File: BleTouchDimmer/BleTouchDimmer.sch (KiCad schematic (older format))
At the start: 12 parts, among them P1 PROG, P2 UART, U2 MDBT40, Y2 Crystal

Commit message: Added triacs.
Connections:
- wire segments 59 -> 55
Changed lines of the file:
@@
 	3650 3550 3650 3600
 $Comp
-L GND #PWR2
+L GND #PWR01
 U 1 1 57955487
 P 3100 3950
-F 0 "#PWR2" H 3100 3700 50  0001 C CNN
+F 0 "#PWR01" H 3100 3700 50  0001 C CNN
 F 1 "GND" H 3100 3800 50  0000 C CNN
 F 2 "" H 3100 3950 50  0000 C CNN
@@
 $EndComp
 Wire Wire Line
-	3250 4100 3250 3850
-Wire Wire Line
-	3250 3850 3250 3550
+	3250 3550 3250 4100
 Wire Wire Line
 	3100 3850 3250 3850
@@
 $EndComp
 $Comp
-L GND #PWR4
+L GND #PWR02
 U 1 1 581A3066
 P 4250 2800
-F 0 "#PWR4" H 4250 2550 50  0001 C CNN
+F 0 "#PWR02" H 4250 2550 50  0001 C CNN
 F 1 "GND" H 4250 2650 50  0000 C CNN
 F 2 "" H 4250 2800 50  0000 C CNN
@@
 $EndComp
 $Comp
-L GND #PWR10
+L GND #PWR03
 U 1 1 581A31E1
 P 6950 2650
-F 0 "#PWR10" H 6950 2400 50  0001 C CNN
+F 0 "#PWR03" H 6950 2400 50  0001 C CNN
 F 1 "GND" H 6950 2500 50  0000 C CNN
 F 2 "" H 6950 2650 50  0000 C CNN
@@
 	4400 2650 4250 2650
 Wire Wire Line
-	4250 2650 4250 2750
-Wire Wire Line
-	4250 2750 4250 2800
+	4250 2650 4250 2800
 Wire Wire Line
 	4400 2750 4250 2750
@@
 	3100 3850 3100 3950
 $Comp
-L GND #PWR5
+L GND #PWR04
 U 1 1 581A7CB9
 P 5000 4750
-F 0 "#PWR5" H 5000 4500 50  0001 C CNN
+F 0 "#PWR04" H 5000 4500 50  0001 C CNN
 F 1 "GND" H 5000 4600 50  0000 C CNN
 F 2 "" H 5000 4750 50  0000 C CNN
@@
 	5000 4550 5000 4750
 $Comp
-L GND #PWR8
+L GND #PWR05
 U 1 1 581A7D2A
 P 6200 4750
-F 0 "#PWR8" H 6200 4500 50  0001 C CNN
+F 0 "#PWR05" H 6200 4500 50  0001 C CNN
 F 1 "GND" H 6200 4600 50  0000 C CNN
 F 2 "" H 6200 4750 50  0000 C CNN
@@
 	6200 4550 6200 4750
 $Comp
-L GND #PWR7
+L GND #PWR06
 U 1 1 581A884C
 P 5000 5900
-F 0 "#PWR7" H 5000 5650 50  0001 C CNN
+F 0 "#PWR06" H 5000 5650 50  0001 C CNN
 F 1 "GND" H 5000 5750 50  0000 C CNN
 F 2 "" H 5000 5900 50  0000 C CNN
@@
 	5000 5800 5000 5900
 $Comp
-L GND #PWR1
+L GND #PWR07
 U 1 1 581ABEA9
 P 3100 3200
-F 0 "#PWR1" H 3100 2950 50  0001 C CNN
+F 0 "#PWR07" H 3100 2950 50  0001 C CNN
 F 1 "GND" H 3100 3050 50  0000 C CNN
 F 2 "" H 3100 3200 50  0000 C CNN
@@
 $EndComp
 Wire Wire Line
-	4400 3100 3850 3100
-Wire Wire Line
-	3850 3100 3550 3100
+	3550 3100 4400 3100
 Wire Wire Line
 	3250 3100 3100 3100
@@
 	3100 3100 3100 3200
 $Comp
-L +3.3V #PWR6
+L +3.3V #PWR08
 U 1 1 581AC6F3
 P 5000 5350
-F 0 "#PWR6" H 5000 5200 50  0001 C CNN
+F 0 "#PWR08" H 5000 5200 50  0001 C CNN
 F 1 "+3.3V" H 5000 5490 50  0000 C CNN
 F 2 "" H 5000 5350 50  0000 C CNN
@@
 $EndComp
 Wire Wire Line
-	5000 5350 5000 5450
-Wire Wire Line
-	5000 5450 5000 5500
+	5000 5350 5000 5500
 Wire Wire Line
 	5100 4550 5100 5450
@@
 Connection ~ 5000 5450
 $Comp
-L +3.3V #PWR3
+L +3.3V #PWR09
 U 1 1 581E4E9B
 P 3850 3050
-F 0 "#PWR3" H 3850 2900 50  0001 C CNN
+F 0 "#PWR09" H 3850 2900 50  0001 C CNN
 F 1 "+3.3V" H 3850 3190 50  0000 C CNN
 F 2 "" H 3850 3050 50  0000 C CNN
@@
 	7800 3850 7800 4000
 $Comp
-L GND #PWR11
+L GND #PWR010
 U 1 1 581AB091
 P 7800 4000
-F 0 "#PWR11" H 7800 3750 50  0001 C CNN
+F 0 "#PWR010" H 7800 3750 50  0001 C CNN
 F 1 "GND" H 7800 3850 50  0000 C CNN
 F 2 "" H 7800 4000 50  0000 C CNN
@@
 SWDIO/RESET
 $Comp
-L +3.3V #PWR12
+L +3.3V #PWR011
 U 1 1 581E9153
 P 9000 3200
-F 0 "#PWR12" H 9000 3050 50  0001 C CNN
+F 0 "#PWR011" H 9000 3050 50  0001 C CNN
 F 1 "+3.3V" H 9000 3340 50  0000 C CNN
 F 2 "" H 9000 3200 50  0000 C CNN
@@
 	9000 3200 9000 3250
 $Comp
-L GND #PWR13
+L GND #PWR012
 U 1 1 581E91BB
 P 9000 3600
-F 0 "#PWR13" H 9000 3350 50  0001 C CNN
+F 0 "#PWR012" H 9000 3350 50  0001 C CNN
 F 1 "GND" H 9000 3450 50  0000 C CNN
 F 2 "" H 9000 3600 50  0000 C CNN
@@
 TX
 $Comp
-L GND #PWR16
+L GND #PWR013
 U 1 1 581EB2A9
 P 9200 5150
-F 0 "#PWR16" H 9200 4900 50  0001 C CNN
+F 0 "#PWR013" H 9200 4900 50  0001 C CNN
 F 1 "GND" H 9200 5000 50  0000 C CNN
 F 2 "" H 9200 5150 50  0000 C CNN
@@
 	10050 4800 9200 4800
 $Comp
-L +3.3V #PWR15
+L +3.3V #PWR014
 U 1 1 581EB479
 P 9200 4750
-F 0 "#PWR15" H 9200 4600 50  0001 C CNN
+F 0 "#PWR014" H 9200 4600 50  0001 C CNN
 F 1 "+3.3V" H 9200 4890 50  0000 C CNN
 F 2 "" H 9200 4750 50  0000 C CNN
@@
 	9000 4850 9000 4900
 $Comp
-L +3.3V #PWR14
+L +3.3V #PWR015
 U 1 1 581EE473
 P 9000 4500
-F 0 "#PWR14" H 9000 4350 50  0001 C CNN
+F 0 "#PWR015" H 9000 4350 50  0001 C CNN
 F 1 "+3.3V" H 9000 4640 50  0000 C CNN
 F 2 "" H 9000 4500 50  0000 C CNN
@@
 	6900 4650 6900 4750
 $Comp
-L GND #PWR9
+L GND #PWR016
 U 1 1 581F1D57
 P 6900 5250
-F 0 "#PWR9" H 6900 5000 50  0001 C CNN
+F 0 "#PWR016" H 6900 5000 50  0001 C CNN
 F 1 "GND" H 6900 5100 50  0000 C CNN
 F 2 "" H 6900 5250 50  0000 C CNN
@@
 ZC_DETECT
 $Comp
-L PWR_FLAG #FLG1
+L PWR_FLAG #FLG017
 U 1 1 581FAA9C
 P 10450 850
-F 0 "#FLG1" H 10450 945 50  0001 C CNN
+F 0 "#FLG017" H 10450 945 50  0001 C CNN
 F 1 "PWR_FLAG" H 10450 1030 50  0000 C CNN
 F 2 "" H 10450 850 50  0000 C CNN
@@
 $EndComp
 $Comp
-L GND #PWR17
+L GND #PWR018
 U 1 1 581FAAED
 P 10450 1150
-F 0 "#PWR17" H 10450 900 50  0001 C CNN
+F 0 "#PWR018" H 10450 900 50  0001 C CNN
 F 1 "GND" H 10450 1000 50  0000 C CNN
 F 2 "" H 10450 1150 50  0000 C CNN
@@
 $EndComp
 $Comp
-L +3.3V #PWR18
+L +3.3V #PWR019
 U 1 1 581FAB37
 P 10800 850
-F 0 "#PWR18" H 10800 700 50  0001 C CNN
+F 0 "#PWR019" H 10800 700 50  0001 C CNN
 F 1 "+3.3V" H 10800 990 50  0000 C CNN
 F 2 "" H 10800 850 50  0000 C CNN
@@
 $EndComp
 $Comp
-L PWR_FLAG #FLG2
+L PWR_FLAG #FLG020
 U 1 1 581FAB81
 P 10800 1100
-F 0 "#FLG2" H 10800 1195 50  0001 C CNN
+F 0 "#FLG020" H 10800 1195 50  0001 C CNN
 F 1 "PWR_FLAG" H 10800 1280 50  0000 C CNN
 F 2 "" H 10800 1100 50  0000 C CNN
@@
 F0 "TRIACS" 60
 F1 "TRIACS.sch" 60
+F2 "TRIAC1_CONTROL" I L 2700 5450 60
+F3 "230VAC_L" I R 3950 5750 60
+F4 "TRIAC1_L_OUT" I R 3950 5900 60
+F5 "TRIAC2_CONTROL" I L 2700 5600 60
+F6 "TRIAC2_L_OUT" I R 3950 6050 60
 $EndSheet
 $EndSCHEMATC

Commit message: Added terminal block.
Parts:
- added P3: POWER, Terminal_Blocks:TerminalBlock_Pheonix_MKDS1.5-4pol, symbol CONN_01X04
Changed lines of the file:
@@
 F6 "TRIAC2_L_OUT" I R 3950 6050 60
 $EndSheet
+$Comp
+L CONN_01X04 P3
+U 1 1 5823D05F
+P 1950 4100
+F 0 "P3" H 1950 4350 50  0000 C CNN
+F 1 "POWER" V 2050 4100 50  0000 C CNN
+F 2 "Terminal_Blocks:TerminalBlock_Pheonix_MKDS1.5-4pol" H 1950 4100 50  0001 C CNN
+F 3 "http://www.mouser.com/ds/2/418/NG_CD_282837_G3-625767.pdf" H 1950 4100 50  0001 C CNN
+F 4 "http://www.mouser.ee/ProductDetail/TE-Connectivity/282837-4/?qs=sGAEpiMZZMvZTcaMAxB2AJ%2f79sE4hFAYNPaLlOiyu2A%3d" H 1950 4100 60  0001 C CNN "Ordering"
+	1    1950 4100
+	-1   0    0    -1
+$EndComp
 $EndSCHEMATC

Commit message: Added comments about possible power supply solutions.
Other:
- note added: "TODO\nPOWERSUPPLY\nPROTECTION\nENCODER/TOUCHWHEEL"
- note added: "http://electronics.stackexchange.com/questions/101818/surface-mount-transformerless-230v-to-3-3v-on-a-small-board"
- note added: "http://electronics.stackexchange.com/questions/67295/converting-universal-ac-to-3-3v-dc-0-1a"
- note added: "http://www.mouser.ee/Semiconductors/Power-Management-ICs/AC-DC-Converters/_/N-64puj/?Ns=Pricing|0"
- note added: "http://www.promelec.ru/pdf/lnk501.pdf"
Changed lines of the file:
@@
 	-1   0    0    -1
 $EndComp
+Text Notes 1100 1800 0    60   Italic 12
+TODO\nPOWERSUPPLY\nPROTECTION\nENCODER/TOUCHWHEEL
+Text Notes 1050 2200 0    60   Italic 12
+http://electronics.stackexchange.com/questions/101818/surface-mount-transformerless-230v-to-3-3v-on-a-small-board
+Text Notes 1050 2350 0    60   Italic 12
+http://electronics.stackexchange.com/questions/67295/converting-universal-ac-to-3-3v-dc-0-1a
+Text Notes 1000 2500 0    60   Italic 12
+http://www.promelec.ru/pdf/lnk501.pdf
+Text Notes 1100 2050 0    60   Italic 12
+http://www.mouser.ee/Semiconductors/Power-Management-ICs/AC-DC-Converters/_/N-64puj/?Ns=Pricing|0
 $EndSCHEMATC

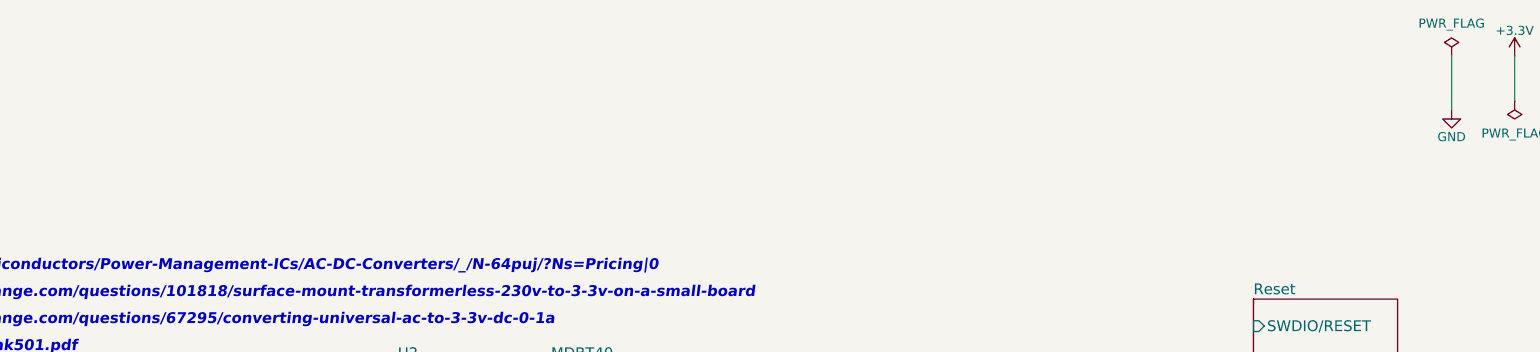
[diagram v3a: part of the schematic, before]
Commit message: Added power supply link LNK4002S.
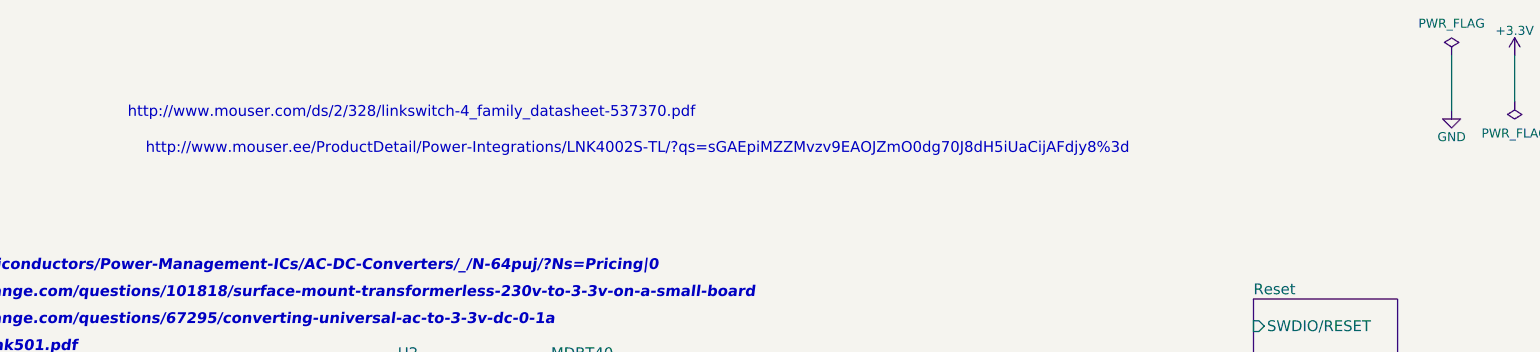
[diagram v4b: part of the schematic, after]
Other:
- note added: "http://www.mouser.com/ds/2/328/linkswitch-4_family_datasheet-537370.pdf"
- note added: "http://www.mouser.ee/ProductDetail/Power-Integrations/LNK4002S-TL/?qs=sGAEpiMZZMvzv9EAOJZmO0dg70J8dH5iUaCijAFdjy8%3d"
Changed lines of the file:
@@
 Text Notes 1100 2050 0    60   Italic 12
 http://www.mouser.ee/Semiconductors/Power-Management-ICs/AC-DC-Converters/_/N-64puj/?Ns=Pricing|0
+Text Notes 3100 1200 0    60   ~ 0
+http://www.mouser.com/ds/2/328/linkswitch-4_family_datasheet-537370.pdf
+Text Notes 3200 1400 0    60   ~ 0
+http://www.mouser.ee/ProductDetail/Power-Integrations/LNK4002S-TL/?qs=sGAEpiMZZMvzv9EAOJZmO0dg70J8dH5iUaCijAFdjy8%3d
 $EndSCHEMATC

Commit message: ADDED LNK4002S
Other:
- note removed: "http://electronics.stackexchange.com/questions/101818/surface-mount-transformerless-230v-to-3-3v-on-a-small-board"
- note removed: "http://electronics.stackexchange.com/questions/67295/converting-universal-ac-to-3-3v-dc-0-1a"
- note removed: "http://www.mouser.com/ds/2/328/linkswitch-4_family_datasheet-537370.pdf"
- note removed: "http://www.mouser.ee/ProductDetail/Power-Integrations/LNK4002S-TL/?qs=sGAEpiMZZMvzv9EAOJZmO0dg70J8dH5iUaCijAFdjy8%3d"
- note removed: "http://www.mouser.ee/Semiconductors/Power-Management-ICs/AC-DC-Converters/_/N-64puj/?Ns=Pricing|0"
- note removed: "http://www.promelec.ru/pdf/lnk501.pdf"
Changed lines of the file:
@@
 LIBS:Egert
 LIBS:Oscillators
+LIBS:74xgxx
+LIBS:ac-dc
+LIBS:actel
+LIBS:Altera
+LIBS:analog_devices
+LIBS:battery_management
+LIBS:bbd
+LIBS:brooktre
+LIBS:cmos_ieee
+LIBS:dc-dc
+LIBS:diode
+LIBS:elec-unifil
+LIBS:ESD_Protection
+LIBS:ftdi
+LIBS:gennum
+LIBS:graphic
+LIBS:hc11
+LIBS:ir
+LIBS:Lattice
+LIBS:logo
+LIBS:maxim
+LIBS:microchip_dspic33dsc
+LIBS:microchip_pic10mcu
+LIBS:microchip_pic12mcu
+LIBS:microchip_pic16mcu
+LIBS:microchip_pic18mcu
+LIBS:microchip_pic32mcu
+LIBS:motor_drivers
+LIBS:motors
+LIBS:msp430
+LIBS:nxp_armmcu
+LIBS:onsemi
+LIBS:Power_Management
+LIBS:powerint
+LIBS:pspice
+LIBS:references
+LIBS:relays
+LIBS:rfcom
+LIBS:sensors
+LIBS:silabs
+LIBS:stm8
+LIBS:stm32
+LIBS:supertex
+LIBS:switches
+LIBS:transf
+LIBS:ttl_ieee
+LIBS:video
+LIBS:wiznet
+LIBS:Worldsemi
+LIBS:Xicor
+LIBS:Zilog
 LIBS:BleTouchDimmer-cache
 EELAYER 25 0
@@
 $Descr A4 11693 8268
 encoding utf-8
-Sheet 1 4
+Sheet 1 5
 Title ""
 Date ""
@@
 	-1   0    0    -1
 $EndComp
-Text Notes 1100 1800 0    60   Italic 12
+Text Notes 800  950  0    60   Italic 12
 TODO\nPOWERSUPPLY\nPROTECTION\nENCODER/TOUCHWHEEL
-Text Notes 1050 2200 0    60   Italic 12
-http://electronics.stackexchange.com/questions/101818/surface-mount-transformerless-230v-to-3-3v-on-a-small-board
-Text Notes 1050 2350 0    60   Italic 12
-http://electronics.stackexchange.com/questions/67295/converting-universal-ac-to-3-3v-dc-0-1a
-Text Notes 1000 2500 0    60   Italic 12
-http://www.promelec.ru/pdf/lnk501.pdf
-Text Notes 1100 2050 0    60   Italic 12
-http://www.mouser.ee/Semiconductors/Power-Management-ICs/AC-DC-Converters/_/N-64puj/?Ns=Pricing|0
-Text Notes 3100 1200 0    60   ~ 0
-http://www.mouser.com/ds/2/328/linkswitch-4_family_datasheet-537370.pdf
-Text Notes 3200 1400 0    60   ~ 0
-http://www.mouser.ee/ProductDetail/Power-Integrations/LNK4002S-TL/?qs=sGAEpiMZZMvzv9EAOJZmO0dg70J8dH5iUaCijAFdjy8%3d
+$Sheet
+S 2650 1150 1150 850
+U 582628CE
+F0 "POWER_SUPPLY" 60
+F1 "POWER_SUPPLY.sch" 60
+$EndSheet
 $EndSCHEMATC

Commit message: Updated power supply with LDO LD1117. TODO - Protection (VARISTOR, ??)
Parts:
- D1: footprint LEDs:LED_0805 -> Resistors_SMD:R_0603_HandSoldering
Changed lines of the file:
@@
 	3650 3550 3650 3600
 $Comp
-L GND #PWR2
+L GND #PWR01
 U 1 1 57955487
 P 3100 3950
-F 0 "#PWR2" H 3100 3700 50  0001 C CNN
+F 0 "#PWR01" H 3100 3700 50  0001 C CNN
 F 1 "GND" H 3100 3800 50  0000 C CNN
 F 2 "" H 3100 3950 50  0000 C CNN
@@
 $EndComp
 $Comp
-L GND #PWR4
+L GND #PWR02
 U 1 1 581A3066
 P 4250 2800
-F 0 "#PWR4" H 4250 2550 50  0001 C CNN
+F 0 "#PWR02" H 4250 2550 50  0001 C CNN
 F 1 "GND" H 4250 2650 50  0000 C CNN
 F 2 "" H 4250 2800 50  0000 C CNN
@@
 $EndComp
 $Comp
-L GND #PWR10
+L GND #PWR03
 U 1 1 581A31E1
 P 6950 2650
-F 0 "#PWR10" H 6950 2400 50  0001 C CNN
+F 0 "#PWR03" H 6950 2400 50  0001 C CNN
 F 1 "GND" H 6950 2500 50  0000 C CNN
 F 2 "" H 6950 2650 50  0000 C CNN
@@
 	3100 3850 3100 3950
 $Comp
-L GND #PWR5
+L GND #PWR04
 U 1 1 581A7CB9
 P 5000 4750
-F 0 "#PWR5" H 5000 4500 50  0001 C CNN
+F 0 "#PWR04" H 5000 4500 50  0001 C CNN
 F 1 "GND" H 5000 4600 50  0000 C CNN
 F 2 "" H 5000 4750 50  0000 C CNN
@@
 	5000 4550 5000 4750
 $Comp
-L GND #PWR8
+L GND #PWR05
 U 1 1 581A7D2A
 P 6200 4750
-F 0 "#PWR8" H 6200 4500 50  0001 C CNN
+F 0 "#PWR05" H 6200 4500 50  0001 C CNN
 F 1 "GND" H 6200 4600 50  0000 C CNN
 F 2 "" H 6200 4750 50  0000 C CNN
@@
 	6200 4550 6200 4750
 $Comp
-L GND #PWR7
+L GND #PWR06
 U 1 1 581A884C
 P 5000 5900
-F 0 "#PWR7" H 5000 5650 50  0001 C CNN
+F 0 "#PWR06" H 5000 5650 50  0001 C CNN
 F 1 "GND" H 5000 5750 50  0000 C CNN
 F 2 "" H 5000 5900 50  0000 C CNN
@@
 	5000 5800 5000 5900
 $Comp
-L GND #PWR1
+L GND #PWR07
 U 1 1 581ABEA9
 P 3100 3200
-F 0 "#PWR1" H 3100 2950 50  0001 C CNN
+F 0 "#PWR07" H 3100 2950 50  0001 C CNN
 F 1 "GND" H 3100 3050 50  0000 C CNN
 F 2 "" H 3100 3200 50  0000 C CNN
@@
 	3100 3100 3100 3200
 $Comp
-L +3.3V #PWR6
+L +3.3V #PWR08
 U 1 1 581AC6F3
 P 5000 5350
-F 0 "#PWR6" H 5000 5200 50  0001 C CNN
+F 0 "#PWR08" H 5000 5200 50  0001 C CNN
 F 1 "+3.3V" H 5000 5490 50  0000 C CNN
 F 2 "" H 5000 5350 50  0000 C CNN
@@
 Connection ~ 5000 5450
 $Comp
-L +3.3V #PWR3
+L +3.3V #PWR09
 U 1 1 581E4E9B
 P 3850 3050
-F 0 "#PWR3" H 3850 2900 50  0001 C CNN
+F 0 "#PWR09" H 3850 2900 50  0001 C CNN
 F 1 "+3.3V" H 3850 3190 50  0000 C CNN
 F 2 "" H 3850 3050 50  0000 C CNN
@@
 	7800 3850 7800 4000
 $Comp
-L GND #PWR11
+L GND #PWR010
 U 1 1 581AB091
 P 7800 4000
-F 0 "#PWR11" H 7800 3750 50  0001 C CNN
+F 0 "#PWR010" H 7800 3750 50  0001 C CNN
 F 1 "GND" H 7800 3850 50  0000 C CNN
 F 2 "" H 7800 4000 50  0000 C CNN
@@
 SWDIO/RESET
 $Comp
-L +3.3V #PWR12
+L +3.3V #PWR011
 U 1 1 581E9153
 P 9000 3200
-F 0 "#PWR12" H 9000 3050 50  0001 C CNN
+F 0 "#PWR011" H 9000 3050 50  0001 C CNN
 F 1 "+3.3V" H 9000 3340 50  0000 C CNN
 F 2 "" H 9000 3200 50  0000 C CNN
@@
 	9000 3200 9000 3250
 $Comp
-L GND #PWR13
+L GND #PWR012
 U 1 1 581E91BB
 P 9000 3600
-F 0 "#PWR13" H 9000 3350 50  0001 C CNN
+F 0 "#PWR012" H 9000 3350 50  0001 C CNN
 F 1 "GND" H 9000 3450 50  0000 C CNN
 F 2 "" H 9000 3600 50  0000 C CNN
@@
 TX
 $Comp
-L GND #PWR16
+L GND #PWR013
 U 1 1 581EB2A9
 P 9200 5150
-F 0 "#PWR16" H 9200 4900 50  0001 C CNN
+F 0 "#PWR013" H 9200 4900 50  0001 C CNN
 F 1 "GND" H 9200 5000 50  0000 C CNN
 F 2 "" H 9200 5150 50  0000 C CNN
@@
 	10050 4800 9200 4800
 $Comp
-L +3.3V #PWR15
+L +3.3V #PWR014
 U 1 1 581EB479
 P 9200 4750
-F 0 "#PWR15" H 9200 4600 50  0001 C CNN
+F 0 "#PWR014" H 9200 4600 50  0001 C CNN
 F 1 "+3.3V" H 9200 4890 50  0000 C CNN
 F 2 "" H 9200 4750 50  0000 C CNN
@@
 	9000 4850 9000 4900
 $Comp
-L +3.3V #PWR14
+L +3.3V #PWR015
 U 1 1 581EE473
 P 9000 4500
-F 0 "#PWR14" H 9000 4350 50  0001 C CNN
+F 0 "#PWR015" H 9000 4350 50  0001 C CNN
 F 1 "+3.3V" H 9000 4640 50  0000 C CNN
 F 2 "" H 9000 4500 50  0000 C CNN
@@
 F 0 "D1" H 6900 5050 50  0000 C CNN
 F 1 "LED" H 6900 4850 50  0000 C CNN
-F 2 "LEDs:LED_0805" H 6900 4950 50  0001 C CNN
+F 2 "Resistors_SMD:R_0603_HandSoldering" H 6900 4950 50  0001 C CNN
 F 3 "" H 6900 4950 50  0000 C CNN
 	1    6900 4950
@@
 	6900 4650 6900 4750
 $Comp
-L GND #PWR9
+L GND #PWR016
 U 1 1 581F1D57
 P 6900 5250
-F 0 "#PWR9" H 6900 5000 50  0001 C CNN
+F 0 "#PWR016" H 6900 5000 50  0001 C CNN
 F 1 "GND" H 6900 5100 50  0000 C CNN
 F 2 "" H 6900 5250 50  0000 C CNN
@@
 ZC_DETECT
 $Comp
-L PWR_FLAG #FLG1
+L PWR_FLAG #FLG017
 U 1 1 581FAA9C
 P 10450 850
-F 0 "#FLG1" H 10450 945 50  0001 C CNN
+F 0 "#FLG017" H 10450 945 50  0001 C CNN
 F 1 "PWR_FLAG" H 10450 1030 50  0000 C CNN
 F 2 "" H 10450 850 50  0000 C CNN
@@
 $EndComp
 $Comp
-L GND #PWR17
+L GND #PWR018
 U 1 1 581FAAED
 P 10450 1150
-F 0 "#PWR17" H 10450 900 50  0001 C CNN
+F 0 "#PWR018" H 10450 900 50  0001 C CNN
 F 1 "GND" H 10450 1000 50  0000 C CNN
 F 2 "" H 10450 1150 50  0000 C CNN
@@
 $EndComp
 $Comp
-L +3.3V #PWR18
+L +3.3V #PWR019
 U 1 1 581FAB37
 P 10800 850
-F 0 "#PWR18" H 10800 700 50  0001 C CNN
+F 0 "#PWR019" H 10800 700 50  0001 C CNN
 F 1 "+3.3V" H 10800 990 50  0000 C CNN
 F 2 "" H 10800 850 50  0000 C CNN
@@
 $EndComp
 $Comp
-L PWR_FLAG #FLG2
+L PWR_FLAG #FLG020
 U 1 1 581FAB81
 P 10800 1100
-F 0 "#FLG2" H 10800 1195 50  0001 C CNN
+F 0 "#FLG020" H 10800 1195 50  0001 C CNN
 F 1 "PWR_FLAG" H 10800 1280 50  0000 C CNN
 F 2 "" H 10800 1100 50  0000 C CNN

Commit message: Added varistor (Small??)
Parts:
- added VR?: VR, Varistors:RV_Disc_D9_W4.4_P5, symbol VR
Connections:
- net labels added: L_IN, N_IN
- wire segments 55 -> 59
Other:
- moved on the sheet: P3
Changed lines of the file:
@@
 L CONN_01X04 P3
 U 1 1 5823D05F
-P 1950 4100
-F 0 "P3" H 1950 4350 50  0000 C CNN
-F 1 "POWER" V 2050 4100 50  0000 C CNN
-F 2 "Terminal_Blocks:TerminalBlock_Pheonix_MKDS1.5-4pol" H 1950 4100 50  0001 C CNN
-F 3 "http://www.mouser.com/ds/2/418/NG_CD_282837_G3-625767.pdf" H 1950 4100 50  0001 C CNN
-F 4 "http://www.mouser.ee/ProductDetail/TE-Connectivity/282837-4/?qs=sGAEpiMZZMvZTcaMAxB2AJ%2f79sE4hFAYNPaLlOiyu2A%3d" H 1950 4100 60  0001 C CNN "Ordering"
-	1    1950 4100
+P 800 4150
+F 0 "P3" H 800 4400 50  0000 C CNN
+F 1 "POWER" V 900 4150 50  0000 C CNN
+F 2 "Terminal_Blocks:TerminalBlock_Pheonix_MKDS1.5-4pol" H 800 4150 50  0001 C CNN
+F 3 "http://www.mouser.com/ds/2/418/NG_CD_282837_G3-625767.pdf" H 800 4150 50  0001 C CNN
+F 4 "http://www.mouser.ee/ProductDetail/TE-Connectivity/282837-4/?qs=sGAEpiMZZMvZTcaMAxB2AJ%2f79sE4hFAYNPaLlOiyu2A%3d" H 800 4150 60  0001 C CNN "Ordering"
+	1    800  4150
 	-1   0    0    -1
 $EndComp
@@
 F1 "POWER_SUPPLY.sch" 60
 $EndSheet
+$Comp
+L VR VR?
+U 1 1 582F67C7
+P 1800 4200
+F 0 "VR?" V 1860 4154 50  0000 C TNN
+F 1 "VR" V 1800 4200 50  0000 C CNN
+F 2 "Varistors:RV_Disc_D9_W4.4_P5" H 1800 4200 50  0001 C CNN
+F 3 "http://www.mouser.ee/ProductDetail/EPCOS-TDK/B72207S0271K101/?qs=sGAEpiMZZMv1TUPJeFpwbucm%252bzz%2f10ZzRDGwdayLxmY%3d" H 1800 4200 50  0001 C CNN
+F 4 "http://www.mouser.com/ds/2/400/SIOV_Leaded_AdvanceD-525613.pdf" V 1800 4200 60  0001 C CNN "Ordering"
+F 5 "275VAC,350DC" V 1800 4200 60  0001 C CNN "Spec"
+	1    1800 4200
+	1    0    0    -1
+$EndComp
+Wire Wire Line
+	1000 4300 1000 4450
+Wire Wire Line
+	1000 4450 1800 4450
+Wire Wire Line
+	1800 3950 1000 3950
+Wire Wire Line
+	1000 3950 1000 4000
+Text Label 1000 3950 0    60   ~ 0
+L_IN
+Text Label 1000 4450 0    60   ~ 0
+N_IN
 $EndSCHEMATC
